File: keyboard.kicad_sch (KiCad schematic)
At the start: 179 parts, among them SW1 SW_Push, SW10 SW_Push, SW11 SW_Push, SW12 SW_Push, SW13 SW_Push, SW14 SW_Push, SW15 SW_Push, SW16 RotaryEncoder, SW17 SW_Push, SW18 SW_Push, SW19 SW_Push, SW2 SW_Push, SW20 SW_Push, SW21 SW_Push, SW22 SW_Push, SW23 SW_Push, SW24 SW_Push, SW25 SW_Push, SW26 SW_Push, SW27 SW_Push, SW28 SW_Push, SW29 SW_Push, SW3 SW_Push, SW30 SW_Push, SW31 SW_Push, SW32 SW_Push, SW33 SW_Push, SW34 SW_Push, SW35 SW_Push, SW36 SW_Push, SW37 SW_Push, SW38 SW_Push, SW39 SW_Push, SW4 SW_Push, SW40 SW_Push, SW41 SW_Push, SW42 SW_Push, SW43 SW_Push, SW44 SW_Push, SW45 SW_Push, SW46 SW_Push, SW47 SW_Push, SW48 SW_Push, SW49 SW_Push, SW5 SW_Push, SW50 SW_Push, SW51 SW_Push, SW52 SW_Push, SW53 SW_Push, SW54 SW_Push, SW55 SW_Push, SW56 SW_Push, SW57 SW_Push, SW58 SW_Push, SW59 SW_Push, SW6 SW_Push, SW60 SW_Push, SW61 SW_Push, SW62 SW_Push, SW63 SW_Push, SW64 SW_Push, SW65 SW_Push, SW66 SW_Push, SW67 SW_Push, SW68 SW_Push, SW69 SW_Push, SW7 SW_Push, SW70 SW_Push, SW71 SW_Push, SW72 SW_Push, SW73 SW_Push, SW74 SW_Push, SW75 SW_Push, SW76 SW_Push, SW77 SW_Push, SW78 SW_Push, SW79 SW_Push, SW8 SW_Push, SW80 SW_Push, SW81 SW_Push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

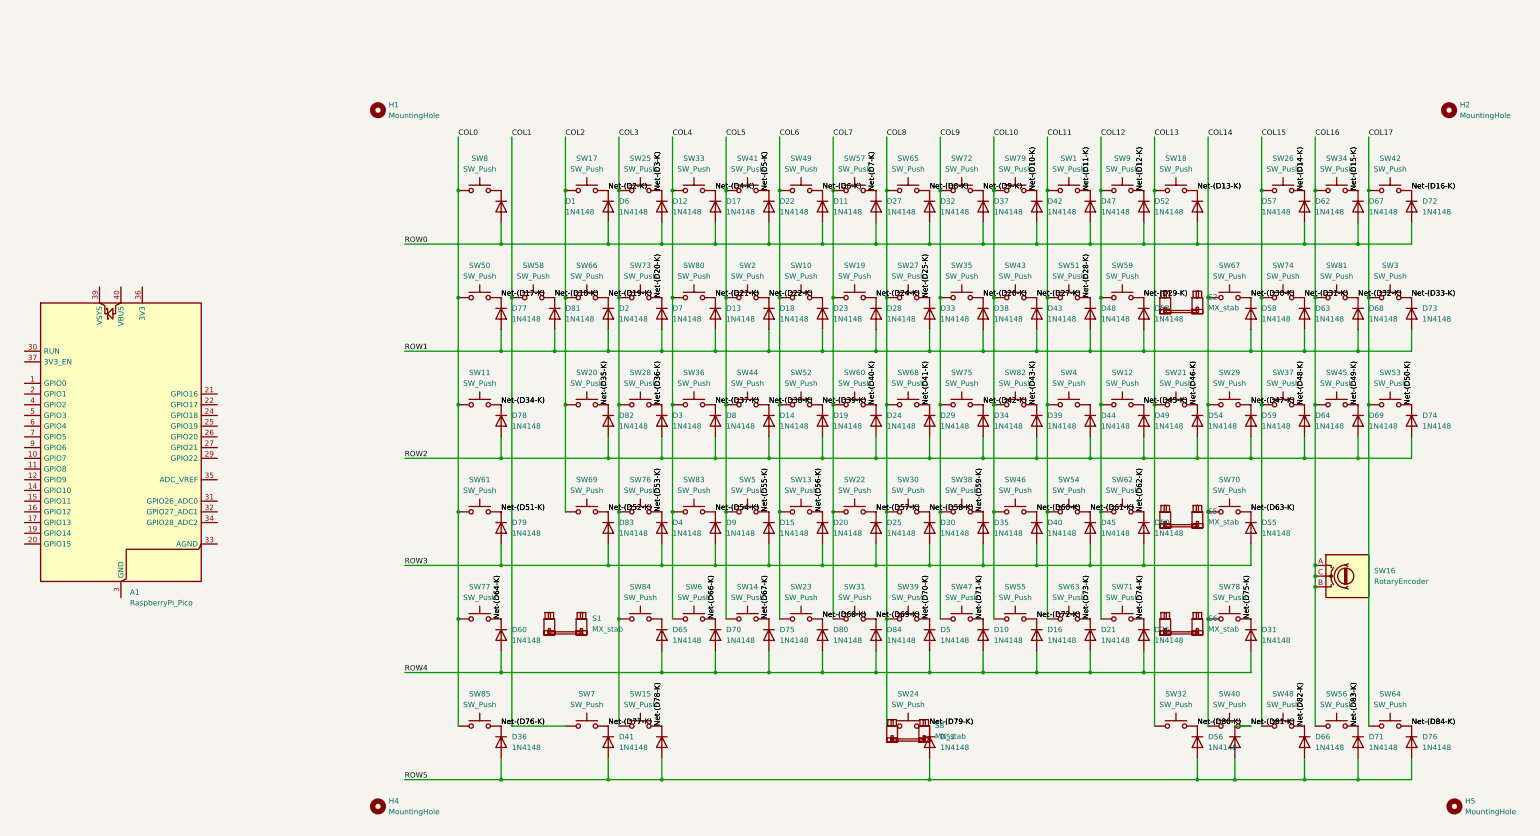
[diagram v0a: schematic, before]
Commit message: Partially fixed layout in pcb
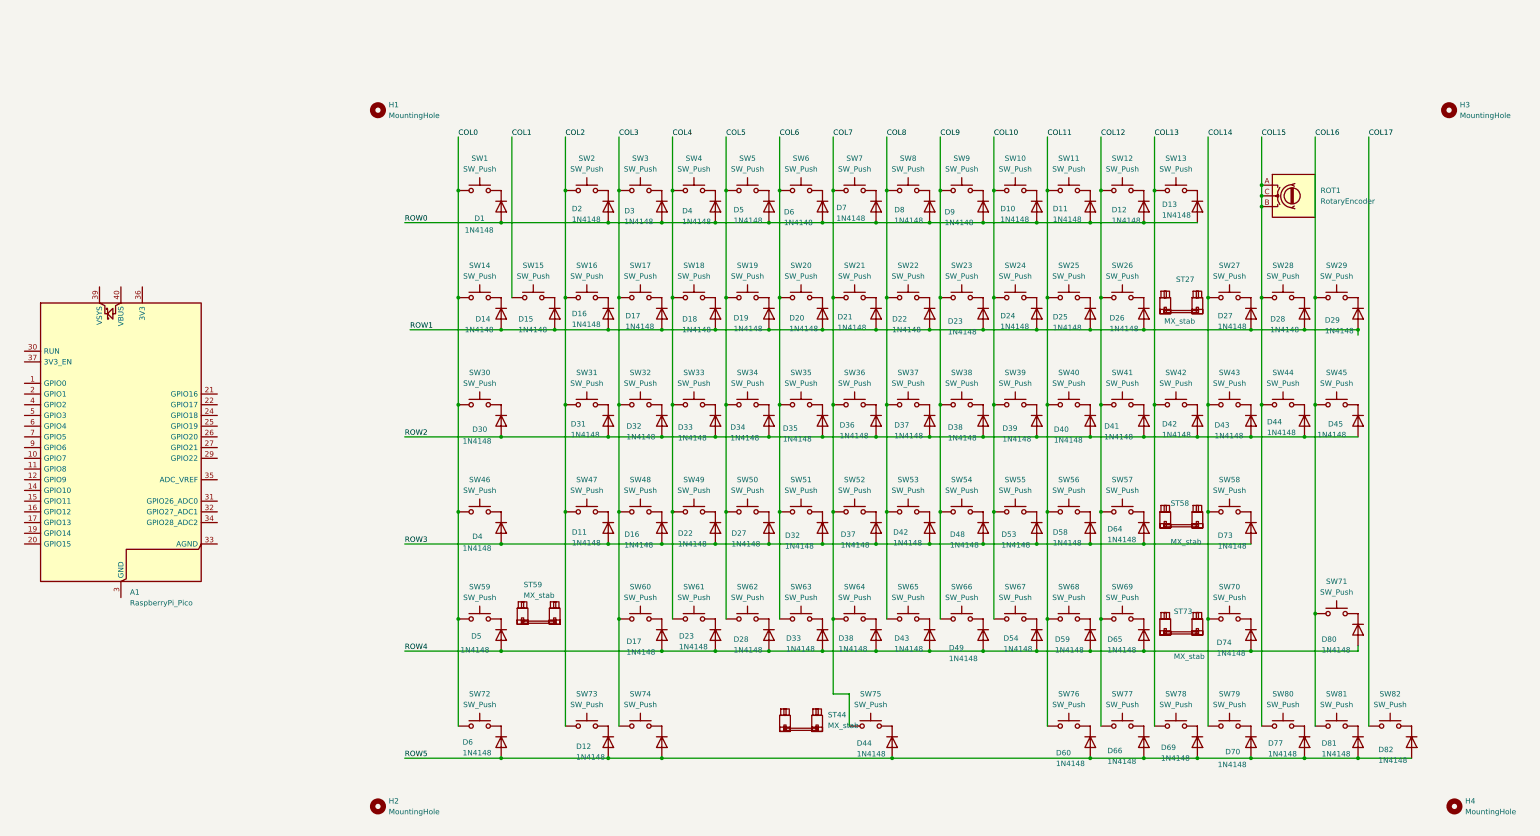
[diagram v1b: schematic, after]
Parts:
- removed D62, D67, D72: 1N4148, Diode_THT:D_DO-35_SOD27_P7.62mm_Horizontal, symbol Diode:1N4148
- removed SW26, SW34, SW42: SW_Push, PCM_marbastlib-mx:SW_MX_1u, symbol Switch:SW_Push
- added D66: 1N4148, Diode_THT:D_DO-35_SOD27_P7.62mm_Horizontal, symbol Diode:1N4148
- added SW77: SW_Push, PCM_marbastlib-mx:SW_MX_1u, symbol Switch:SW_Push
- ST44: renamed from S8; footprint PCM_marbastlib-mx:STAB_MX_P_4u -> PCM_marbastlib-mx:STAB_MX_P_6.25u
- ST58: renamed from S5; footprint PCM_marbastlib-mx:STAB_MX_P_2u -> PCM_marbastlib-mx:STAB_MX_P_2.25u
- ST59: renamed from S1; footprint PCM_marbastlib-mx:STAB_MX_P_3u -> PCM_marbastlib-mx:STAB_MX_P_2.25u
- ST73: renamed from S6; footprint PCM_marbastlib-mx:STAB_MX_P_2u -> PCM_marbastlib-mx:STAB_MX_P_2.75u
- renumbered D42 to D10, D83 to D11, D47 to D11, D52 to D12, D41 to D12, D57 to D13, D77 to D14, D81 to D15, D2 to D16, D4 to D16, D7 to D17, D65 to D17, D13 to D18, D46 to D18, D18 to D19, D6 to D2, D23 to D20, D28 to D21, D9 to D22, D33 to D22, D70 to D23, D38 to D23, D43 to D24, D48 to D25, D53 to D26, D15 to D27, D58 to D27, D63 to D28, D75 to D28, D68 to D29, D12 to D3, D78 to D30, D82 to D31, D3 to D32, D20 to D32, D80 to D33, D8 to D33, D14 to D34, D19 to D35, D24 to D36, D29 to D37, D25 to D37, D84 to D38, D34 to D38, D79 to D4, D17 to D4, D44 to D40, D49 to D41, D54 to D42, D30 to D42, D5 to D43, D59 to D43, D51 to D44, D64 to D44, D69 to D45, D35 to D48, D10 to D49, D22 to D5, D60 to D5, D40 to D53, D16 to D54, D45 to D58, D21 to D59, D11 to D6, D36 to D6, D73 to D60, D50 to D64, D26 to D65, D56 to D69, D27 to D7, D61 to D70, D55 to D73, D31 to D74, D66 to D77, D32 to D8, D74 to D80, D71 to D81, D76 to D82, D37 to D9, H4 to H2, H2 to H3, H5 to H4, SW16 to ROT1, S2 to ST27, SW8 to SW1, SW79 to SW10, SW1 to SW11, SW9 to SW12, SW18 to SW13, SW50 to SW14, SW58 to SW15, SW66 to SW16, SW73 to SW17, SW80 to SW18, SW2 to SW19, SW17 to SW2, SW10 to SW20, SW19 to SW21, SW27 to SW22, SW35 to SW23, SW43 to SW24, SW51 to SW25, SW59 to SW26, SW67 to SW27, SW74 to SW28, SW81 to SW29, SW25 to SW3, SW11 to SW30, SW20 to SW31, SW28 to SW32, SW36 to SW33, SW44 to SW34, SW52 to SW35, SW60 to SW36, SW68 to SW37, SW75 to SW38, SW82 to SW39, SW33 to SW4, SW4 to SW40, SW12 to SW41, SW21 to SW42, SW29 to SW43, SW37 to SW44, SW61 to SW46, SW69 to SW47, SW76 to SW48, SW83 to SW49, SW41 to SW5, SW5 to SW50, SW13 to SW51, SW22 to SW52, SW30 to SW53, SW38 to SW54, SW46 to SW55, SW54 to SW56, SW62 to SW57, SW70 to SW58, SW77 to SW59, SW49 to SW6, SW84 to SW60, SW6 to SW61, SW14 to SW62, SW23 to SW63, SW31 to SW64, SW39 to SW65, SW47 to SW66, SW55 to SW67, SW63 to SW68, SW71 to SW69, SW57 to SW7, SW78 to SW70, SW53 to SW71, SW85 to SW72, SW7 to SW73, SW15 to SW74, SW24 to SW75, SW3 to SW76, SW32 to SW78, SW40 to SW79, SW65 to SW8, SW48 to SW80, SW56 to SW81, SW64 to SW82, SW72 to SW9
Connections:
- net COL1: no longer SW73.1
- net COL11: now also SW76.1
- net COL12: now also SW77.1
- net COL15: now also ROT1.A, ROT1.B, ROT1.C
- net COL16: now also SW71.1; no longer ROT1.A, ROT1.B, ROT1.C
- net COL17: no longer SW71.1, SW76.1
- net COL2: now also SW73.1
- net COL7: now also SW75.1
- net COL8: no longer SW75.1
- net ROW1: no longer D60.2 (A)
- net ROW2: no longer D80.2 (A)
- net ROW4: now also D80.2 (A)
- net ROW5: now also D60.2 (A), D66.2 (A)
- net Net-(D10-K): no longer names the net of D10.1 (K), SW10.2
- net Net-(D11-K): no longer names the net of D11.1 (K), SW11.2
- net Net-(D12-K): no longer names the net of D12.1 (K), SW12.2
- net Net-(D13-K): no longer names the net of D13.1 (K), SW13.2
- net Net-(D17-K): no longer names the net of D14.1 (K), SW14.2
- net Net-(D18-K): no longer names the net of D15.1 (K), SW15.2
- net Net-(D19-K): no longer names the net of D16.1 (K), SW16.2
- net Net-(D2-K): no longer names the net of D2.1 (K), SW2.2
- net Net-(D20-K): no longer names the net of D17.1 (K), SW17.2
- net Net-(D21-K): no longer names the net of D18.1 (K), SW18.2
- net Net-(D22-K): no longer names the net of D19.1 (K), SW19.2
- net Net-(D24-K): no longer names the net of D21.1 (K), SW21.2
- net Net-(D25-K): no longer names the net of D22.1 (K), SW22.2
- net Net-(D26-K): no longer names the net of D23.1 (K), SW23.2
- net Net-(D27-K): no longer names the net of D24.1 (K), SW24.2
- net Net-(D28-K): no longer names the net of D25.1 (K), SW25.2
- net Net-(D29-K): no longer names the net of D26.1 (K), SW26.2
- net Net-(D3-K): no longer names the net of D3.1 (K), SW3.2
- net Net-(D30-K): no longer names the net of D27.1 (K), SW27.2
- net Net-(D31-K): no longer names the net of D28.1 (K), SW28.2
- net Net-(D32-K): no longer names the net of D29.1 (K), SW29.2
- net Net-(D33-K): no longer names the net of D60.1 (K), SW76.2
- net Net-(D34-K): no longer names the net of D30.1 (K), SW30.2
- net Net-(D35-K): no longer names the net of D31.1 (K), SW31.2
- net Net-(D36-K): no longer names the net of D32.1 (K), SW32.2
- net Net-(D37-K): no longer names the net of D33.1 (K), SW33.2
- net Net-(D38-K): no longer names the net of D34.1 (K), SW34.2
- net Net-(D39-K): no longer names the net of D35.1 (K), SW35.2
- net Net-(D4-K): no longer names the net of D4.1 (K), SW4.2
- net Net-(D40-K): no longer names the net of D36.1 (K), SW36.2
- net Net-(D41-K): no longer names the net of D37.1 (K), SW37.2
- net Net-(D42-K): no longer names the net of D38.1 (K), SW38.2
- net Net-(D43-K): no longer names the net of D39.1 (K), SW39.2
- net Net-(D45-K): no longer names the net of D41.1 (K), SW41.2
- net Net-(D46-K): no longer names the net of D42.1 (K), SW42.2
- net Net-(D47-K): no longer names the net of D43.1 (K), SW43.2
- net Net-(D48-K): no longer names the net of D44.1 (K), SW44.2
- net Net-(D49-K): no longer names the net of D45.1 (K), SW45.2
- net Net-(D5-K): no longer names the net of D5.1 (K), SW5.2
- net Net-(D50-K): no longer names the net of D80.1 (K), SW71.2
- net Net-(D51-K): no longer names the net of D4.1 (K), SW46.2
- net Net-(D52-K): no longer names the net of D11.1 (K), SW47.2
- net Net-(D53-K): no longer names the net of D16.1 (K), SW48.2
- net Net-(D54-K): no longer names the net of D22.1 (K), SW49.2
- net Net-(D55-K): no longer names the net of D27.1 (K), SW50.2
- net Net-(D56-K): no longer names the net of D32.1 (K), SW51.2
- net Net-(D57-K): no longer names the net of D37.1 (K), SW52.2
- net Net-(D58-K): no longer names the net of D42.1 (K), SW53.2
- net Net-(D59-K): no longer names the net of D48.1 (K), SW54.2
- net Net-(D6-K): no longer names the net of D6.1 (K), SW6.2
- net Net-(D60-K): no longer names the net of D53.1 (K), SW55.2
- net Net-(D61-K): no longer names the net of D58.1 (K), SW56.2
- net Net-(D62-K): no longer names the net of D64.1 (K), SW57.2
- net Net-(D63-K): no longer names the net of D73.1 (K), SW58.2
- net Net-(D64-K): no longer names the net of D5.1 (K), SW59.2
- net Net-(D66-K): no longer names the net of D23.1 (K), SW61.2
- net Net-(D67-K): no longer names the net of D28.1 (K), SW62.2
- net Net-(D68-K): no longer names the net of D33.1 (K), SW63.2
- net Net-(D69-K): no longer names the net of D38.1 (K), SW64.2
- net Net-(D7-K): no longer names the net of D7.1 (K), SW7.2
- net Net-(D70-K): no longer names the net of D43.1 (K), SW65.2
- net Net-(D71-K): no longer names the net of D49.1 (K), SW66.2
- net Net-(D72-K): no longer names the net of D54.1 (K), SW67.2
- net Net-(D73-K): no longer names the net of D59.1 (K), SW68.2
- net Net-(D74-K): no longer names the net of D65.1 (K), SW69.2
- net Net-(D75-K): no longer names the net of D74.1 (K), SW70.2
- net Net-(D76-K): no longer names the net of D6.1 (K), SW72.2
- net Net-(D77-K): no longer names the net of D12.1 (K), SW73.2
- net Net-(D78-K): no longer names the net of D18.1 (K), SW74.2
- net Net-(D79-K): no longer names the net of D44.1 (K), SW75.2
- net Net-(D8-K): no longer names the net of D8.1 (K), SW8.2
- net Net-(D80-K): no longer names the net of D69.1 (K), SW78.2
- net Net-(D81-K): no longer names the net of D70.1 (K), SW79.2
- net Net-(D82-K): no longer names the net of D77.1 (K), SW80.2
- net Net-(D83-K): no longer names the net of D81.1 (K), SW81.2
- net Net-(D84-K): no longer names the net of D82.1 (K), SW82.2
- net Net-(D9-K): no longer names the net of D9.1 (K), SW9.2
- new net: D66.1 (K), SW77.2
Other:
- moved on the sheet: D44, D60, D80, ROT1, ST44, ST59, SW71, SW75, SW76

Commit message: Added traces in schematic, not completely implemented on pcb
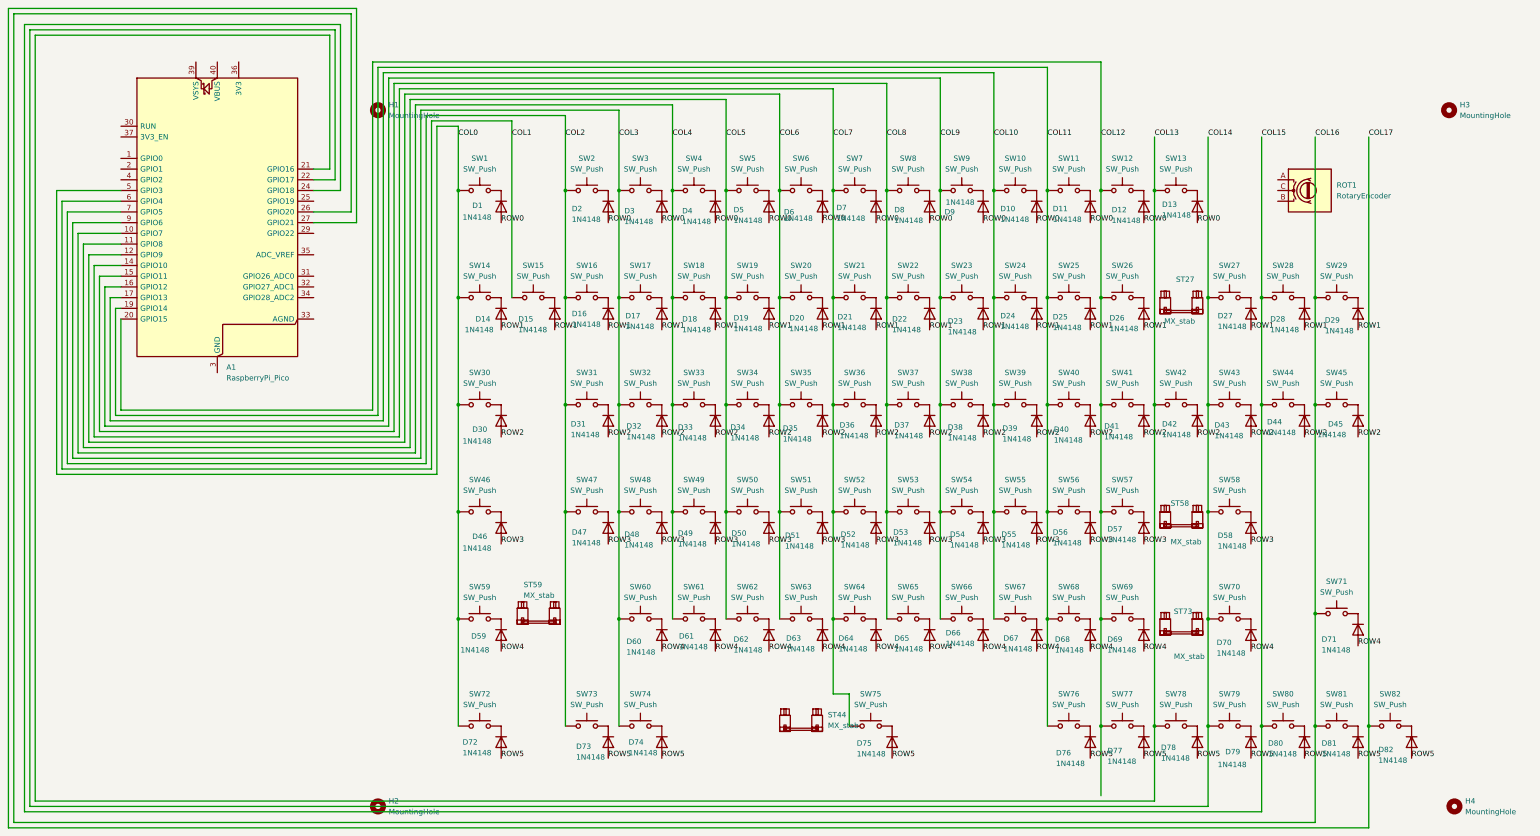
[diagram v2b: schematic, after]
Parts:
- D6: footprint PCM_marbastlib-mx:SW_MX_1u -> Diode_THT:D_DO-35_SOD27_P7.62mm_Horizontal
- renumbered D4 to D46, D11 to D47, D16 to D48, D22 to D49, D27 to D50, D32 to D51, D37 to D52, D42 to D53, D48 to D54, D53 to D55, D58 to D56, D64 to D57, D73 to D58, D5 to D59, D17 to D60, D23 to D61, D28 to D62, D33 to D63, D38 to D64, D43 to D65, D49 to D66, D54 to D67, D59 to D68, D65 to D69, D74 to D70, D80 to D71, D6 to D72, D12 to D73, D18 to D74, D44 to D75, D60 to D76, D66 to D77, D69 to D78, D70 to D79, D77 to D80
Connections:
- net COL0: now also A1.5 (GPIO3)
- net COL1: now also A1.6 (GPIO4)
- net COL10: now also A1.17 (GPIO13)
- net COL11: now also A1.19 (GPIO14)
- net COL12: now also A1.20 (GPIO15)
- net COL13: now also A1.21 (GPIO16)
- net COL14: now also A1.22 (GPIO17)
- net COL15: now also A1.24 (GPIO18); no longer ROT1.A, ROT1.B, ROT1.C
- net COL16: now also A1.26 (GPIO20)
- net COL17: now also A1.27 (GPIO21)
- net COL2: now also A1.7 (GPIO5)
- net COL3: now also A1.9 (GPIO6)
- net COL4: now also A1.10 (GPIO7)
- net COL5: now also A1.11 (GPIO8)
- net COL6: now also A1.12 (GPIO9)
- net COL7: now also A1.14 (GPIO10)
- net COL8: now also A1.15 (GPIO11)
- net COL9: now also A1.16 (GPIO12)
- net ROW0: no longer D6.2 (A)
- net ROW2: no longer D34.2 (A)
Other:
- moved on the sheet: A1, ROT1
